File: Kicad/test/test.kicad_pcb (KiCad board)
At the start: 2 copper layers, 48 x 48 mm, 77 parts, among them J1 SPKOUT, J3 Conn_01x08_Pin, P1 USB_C_Plug_USB2.0, SW2 SW_Push, SW3 SW_Push, SW4 SW_Push, SW5 SW_Push, U1 MAX98357A, U2 ESP32-S3-WROOM-1, U3 OV5640, U4 24Mhz, U5 AXP2101

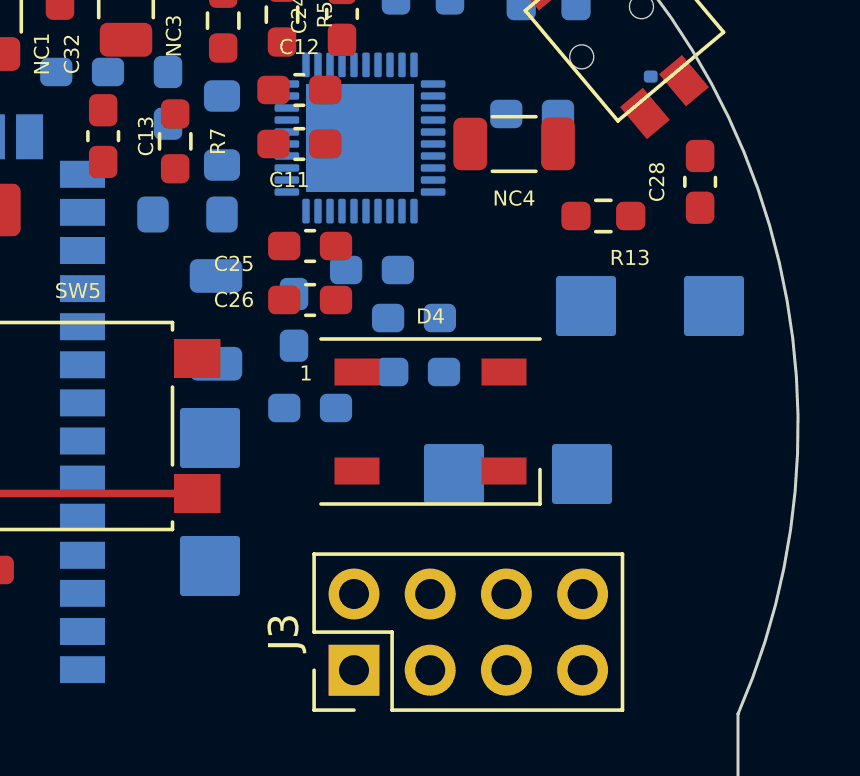
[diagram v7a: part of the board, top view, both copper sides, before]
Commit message: Updated PCB floor
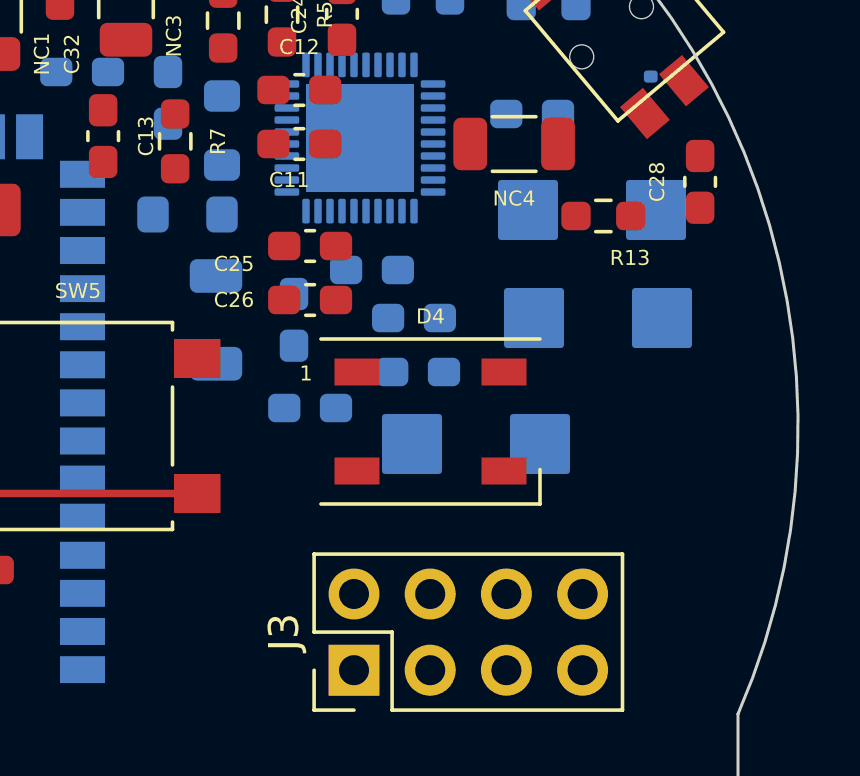
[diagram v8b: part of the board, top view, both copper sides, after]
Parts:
- moved BAT1 16.1 mm to (167.1, 92.7), turned to 0 degrees
- moved 3v3J1 1.78 mm to (167.3, 96.5)
- moved 3v3J2 1.72 mm to (163.3, 100.7)
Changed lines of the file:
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@@
 	(footprint "Footprint_Wareit_Mic:SMD_CONNECTOR_PAD"
 		(layer "B.Cu")
-		(at 169.0664 96.0508 180)
+		(at 167.3336 96.4508 180)
 		(property "Reference" "3v3J1"
 			(at 0.1524 1.1176 0)
@@
 	(footprint "Footprint_Wareit_Mic:SMD_CONNECTOR_PAD"
 		(layer "B.Cu")
-		(at 164.6664 101.6508 180)
+		(at 163.2664 100.6508 180)
 		(property "Reference" "3v3J2"
 			(at 0.1524 1.1176 0)
@@
 	(footprint "Footprint_Wareit_Mic:SMD_CONNECTOR_PAD"
 		(layer "B.Cu")
-		(at 154.3492 102.5336 90)
+		(at 167.1336 92.7492)
 		(property "Reference" "BAT1"
-			(at 0.1524 1.1176 -90)
+			(at 0.1524 1.1176 180)
 			(unlocked yes)
 			(layer "B.SilkS")
@@
 		)
 		(property "Value" "Conn_01x02_Pin"
-			(at 0 -1 -90)
+			(at 0 -1 180)
 			(unlocked yes)
 			(layer "B.Fab")
@@
 		)
 		(property "Footprint" "Footprint_Wareit_Mic:SMD_CONNECTOR_PAD"
-			(at 0 0 -90)
+			(at 0 0 180)
 			(unlocked yes)
 			(layer "B.Fab")
@@
 		)
 		(property "Datasheet" ""
-			(at 0 0 -90)
+			(at 0 0 180)
 			(unlocked yes)
 			(layer "B.Fab")
@@
 		)
 		(property "Description" "Generic connector, single row, 01x02, script generated"
-			(at 0 0 -90)
+			(at 0 0 180)
 			(unlocked yes)
 			(layer "B.Fab")
@@
 		)
 		(fp_text user "${REFERENCE}"
-			(at 0 -2.5 -90)
+			(at 0 -2.5 180)
 			(unlocked yes)
 			(layer "B.Fab")
@@
 		)
 		(pad "1" smd roundrect
-			(at -2.1336 0.0508 90)
+			(at -2.1336 0.0508)
 			(size 2 2)
 			(layers "B.Cu" "B.Paste" "B.Mask")
@@
 		)
 		(pad "2" smd roundrect
-			(at 2.1336 0.0508 90)
+			(at 2.1336 0.0508)
 			(size 2 2)
 			(layers "B.Cu" "B.Paste" "B.Mask")
